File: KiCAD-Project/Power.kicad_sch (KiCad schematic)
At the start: 19 parts, among them U401 DRV8323SRTAR-DRV8323SRTAR

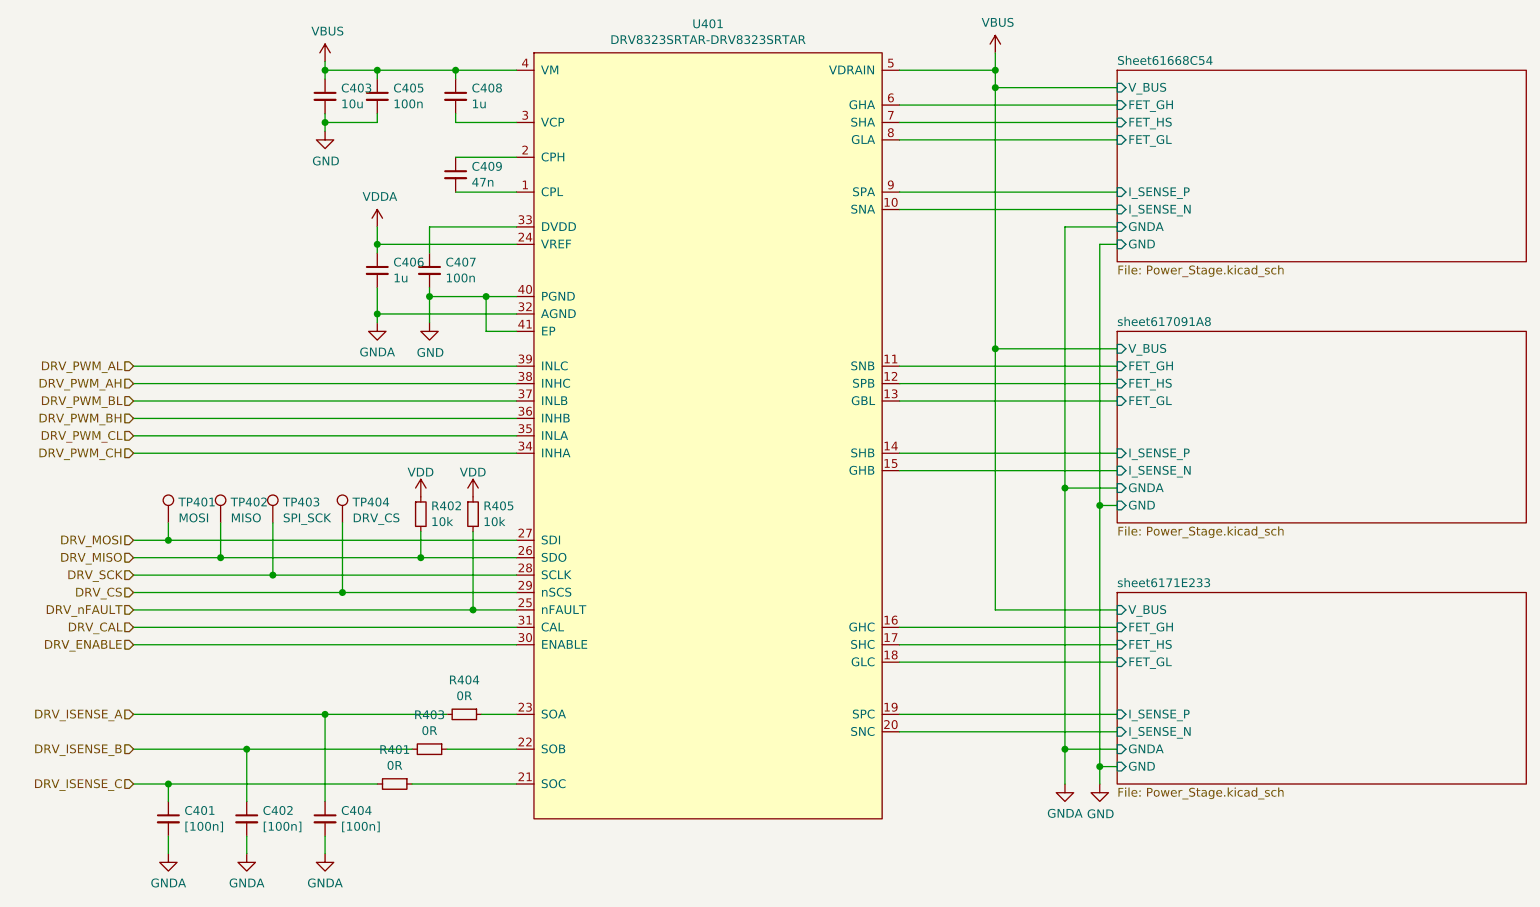
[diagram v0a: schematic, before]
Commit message: DRC resolved
removed GNDA, GNDS from schematic due to no solution was found to get a net-tie in inner layers
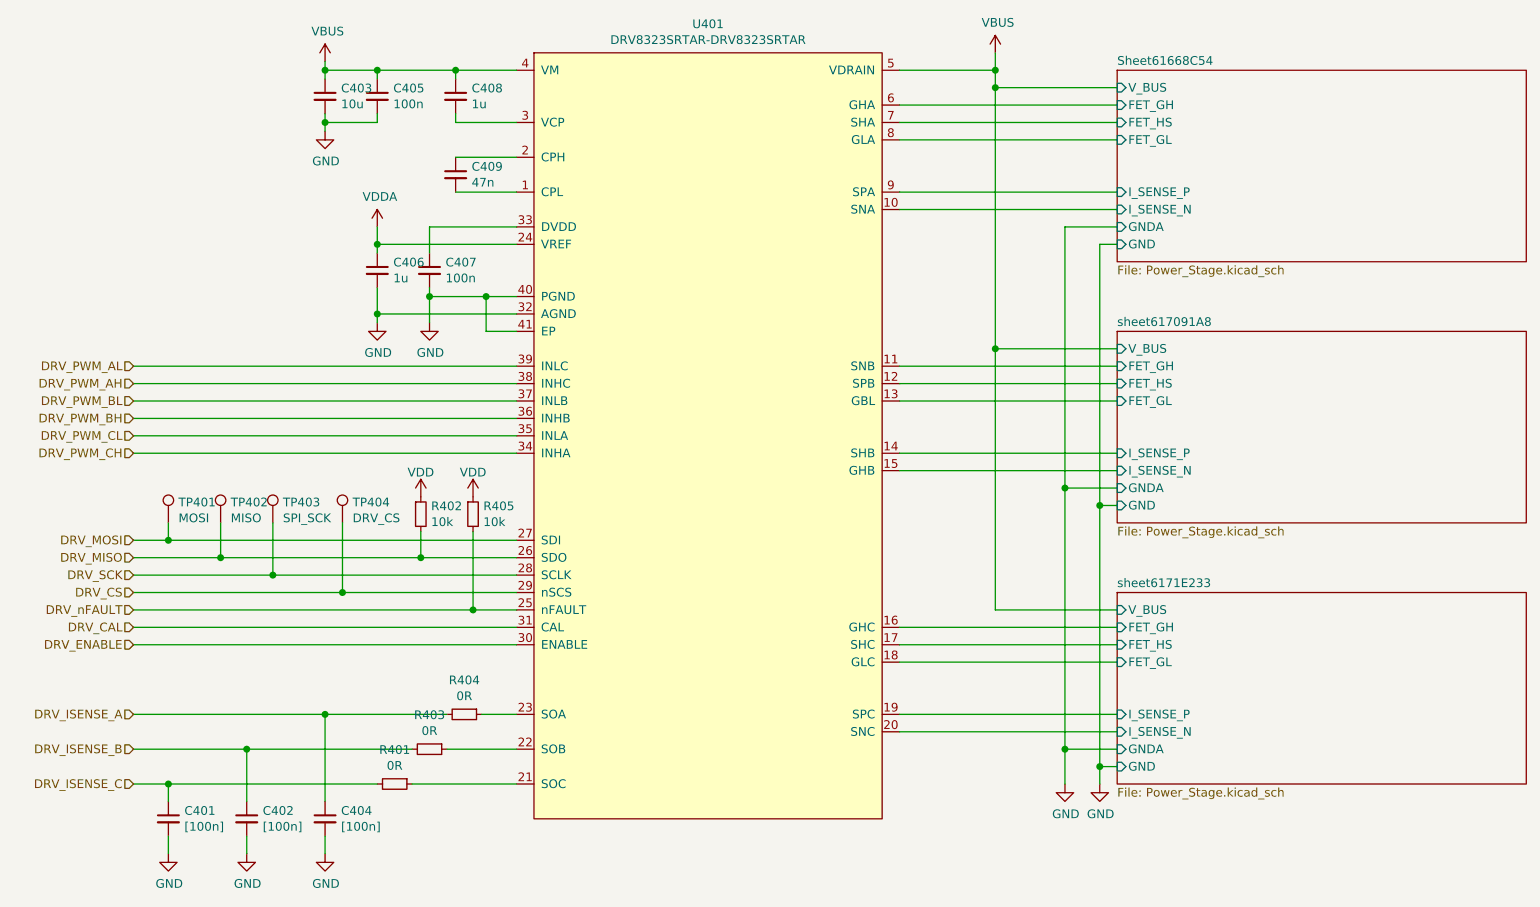
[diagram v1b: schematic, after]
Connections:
- net GNDA is gone; now on net GND: C401.2, C402.2, C404.2, C406.2, U401.32 (AGND)
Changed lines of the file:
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@@
     (pin "1")
   )
-  (symbol (lib_id "power:GNDA") (at 81.28 152.4 0) (unit 1)
-    (in_bom yes) (on_board yes) (fields_autoplaced)
-    (property "Reference" "#PWR0132" (id 0) (at 81.28 158.75 0)
+  (symbol (lib_id "power:GND") (at 81.28 152.4 0) (unit 1)
+    (in_bom yes) (on_board yes)
+    (property "Reference" "#PWR?" (id 0) (at 81.28 158.75 0)
       (effects (font (size 1.27 1.27)) hide)
     )
-    (property "Value" "GNDA" (id 1) (at 81.28 156.7244 0))
+    (property "Value" "GND" (id 1) (at 81.407 156.7942 0))
     (property "Footprint" "" (id 2) (at 81.28 152.4 0)
       (effects (font (size 1.27 1.27)) hide)
@@
     (pin "1")
   )
-  (symbol (lib_id "power:GNDA") (at 92.71 152.4 0) (unit 1)
-    (in_bom yes) (on_board yes) (fields_autoplaced)
-    (property "Reference" "#PWR0133" (id 0) (at 92.71 158.75 0)
+  (symbol (lib_id "power:GND") (at 92.71 152.4 0) (unit 1)
+    (in_bom yes) (on_board yes)
+    (property "Reference" "#PWR?" (id 0) (at 92.71 158.75 0)
       (effects (font (size 1.27 1.27)) hide)
     )
-    (property "Value" "GNDA" (id 1) (at 92.71 156.7244 0))
+    (property "Value" "GND" (id 1) (at 92.837 156.7942 0))
     (property "Footprint" "" (id 2) (at 92.71 152.4 0)
       (effects (font (size 1.27 1.27)) hide)
@@
     (pin "1")
   )
-  (symbol (lib_id "power:GNDA") (at 104.14 152.4 0) (unit 1)
-    (in_bom yes) (on_board yes) (fields_autoplaced)
-    (property "Reference" "#PWR0134" (id 0) (at 104.14 158.75 0)
+  (symbol (lib_id "power:GND") (at 104.14 152.4 0) (unit 1)
+    (in_bom yes) (on_board yes)
+    (property "Reference" "#PWR?" (id 0) (at 104.14 158.75 0)
       (effects (font (size 1.27 1.27)) hide)
     )
-    (property "Value" "GNDA" (id 1) (at 104.14 156.7244 0))
+    (property "Value" "GND" (id 1) (at 104.267 156.7942 0))
     (property "Footprint" "" (id 2) (at 104.14 152.4 0)
       (effects (font (size 1.27 1.27)) hide)
@@
     (pin "1")
   )
-  (symbol (lib_id "power:GNDA") (at 111.76 74.93 0) (unit 1)
-    (in_bom yes) (on_board yes) (fields_autoplaced)
-    (property "Reference" "#PWR0131" (id 0) (at 111.76 81.28 0)
+  (symbol (lib_id "power:GND") (at 111.76 74.93 0) (unit 1)
+    (in_bom yes) (on_board yes)
+    (property "Reference" "#PWR?" (id 0) (at 111.76 81.28 0)
       (effects (font (size 1.27 1.27)) hide)
     )
-    (property "Value" "GNDA" (id 1) (at 111.76 79.2544 0))
+    (property "Value" "GND" (id 1) (at 111.887 79.3242 0))
     (property "Footprint" "" (id 2) (at 111.76 74.93 0)
       (effects (font (size 1.27 1.27)) hide)
@@
     (pin "1")
   )
-  (symbol (lib_id "power:GNDA") (at 212.09 142.24 0) (unit 1)
-    (in_bom yes) (on_board yes) (fields_autoplaced)
-    (property "Reference" "#PWR0101" (id 0) (at 212.09 148.59 0)
+  (symbol (lib_id "power:GND") (at 212.09 142.24 0) (unit 1)
+    (in_bom yes) (on_board yes)
+    (property "Reference" "#PWR?" (id 0) (at 212.09 148.59 0)
       (effects (font (size 1.27 1.27)) hide)
     )
-    (property "Value" "GNDA" (id 1) (at 212.09 146.5644 0))
+    (property "Value" "GND" (id 1) (at 212.217 146.6342 0))
     (property "Footprint" "" (id 2) (at 212.09 142.24 0)
       (effects (font (size 1.27 1.27)) hide)

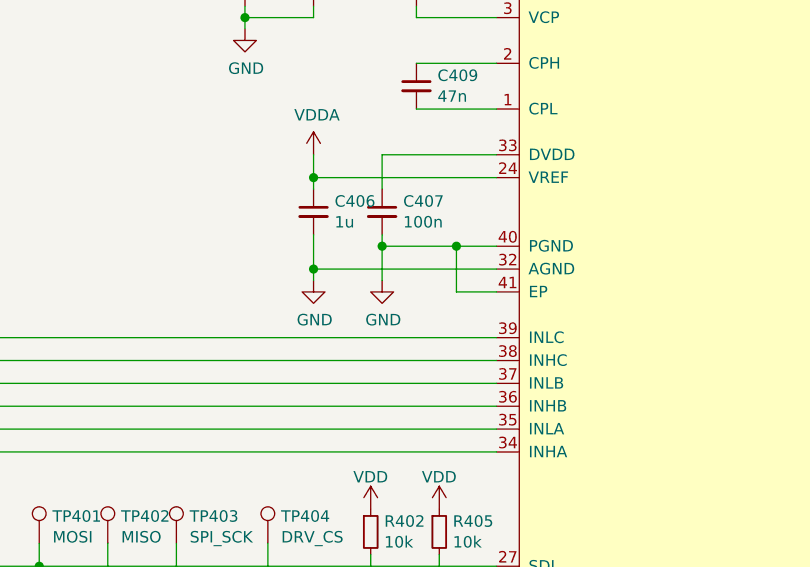
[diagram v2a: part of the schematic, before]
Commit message: changed connectors to THT
changed connectors to THT, removed UART connector
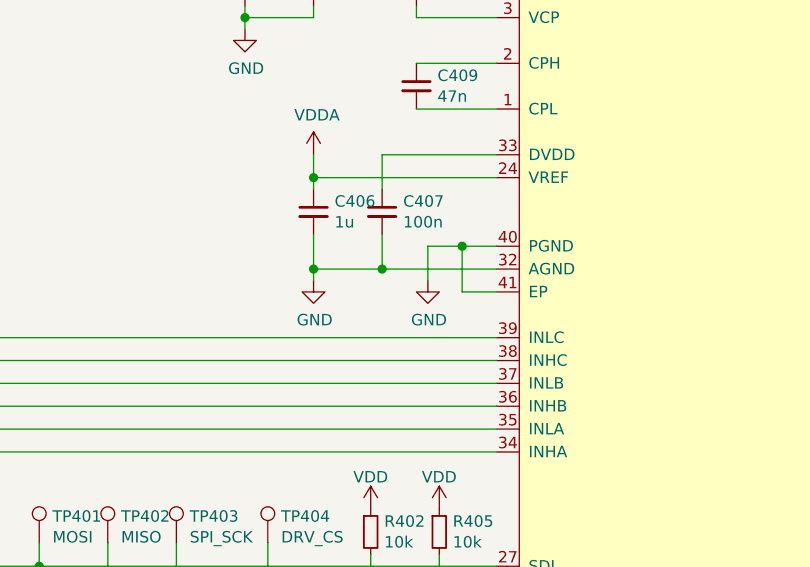
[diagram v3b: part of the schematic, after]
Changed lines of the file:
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@@
   (junction (at 111.76 73.66) (diameter 1.016) (color 0 0 0 0))
   (junction (at 118.11 109.22) (diameter 1.016) (color 0 0 0 0))
-  (junction (at 119.38 71.12) (diameter 1.016) (color 0 0 0 0))
+  (junction (at 119.38 73.66) (diameter 1.016) (color 0 0 0 0))
   (junction (at 123.19 38.1) (diameter 1.016) (color 0 0 0 0))
   (junction (at 125.73 116.84) (diameter 1.016) (color 0 0 0 0))
-  (junction (at 127.635 71.12) (diameter 1.016) (color 0 0 0 0))
+  (junction (at 128.27 71.12) (diameter 1.016) (color 0 0 0 0))
   (junction (at 201.93 38.1) (diameter 1.016) (color 0 0 0 0))
   (junction (at 201.93 40.64) (diameter 1.016) (color 0 0 0 0))
@@
     (stroke (width 0) (type solid) (color 0 0 0 0))
   )
-  (wire (pts (xy 111.76 73.66) (xy 132.08 73.66))
+  (wire (pts (xy 111.76 73.66) (xy 119.38 73.66))
     (stroke (width 0) (type solid) (color 0 0 0 0))
   )
@@
     (stroke (width 0) (type solid) (color 0 0 0 0))
   )
-  (wire (pts (xy 119.38 69.85) (xy 119.38 71.12))
-    (stroke (width 0) (type solid) (color 0 0 0 0))
-  )
-  (wire (pts (xy 119.38 71.12) (xy 119.38 74.93))
-    (stroke (width 0) (type solid) (color 0 0 0 0))
-  )
-  (wire (pts (xy 119.38 71.12) (xy 127.635 71.12))
+  (wire (pts (xy 119.38 69.85) (xy 119.38 73.66))
+    (stroke (width 0) (type solid) (color 0 0 0 0))
+  )
+  (wire (pts (xy 119.38 73.66) (xy 132.08 73.66))
     (stroke (width 0) (type solid) (color 0 0 0 0))
   )
@@
     (stroke (width 0) (type solid) (color 0 0 0 0))
   )
+  (wire (pts (xy 124.46 71.12) (xy 128.27 71.12))
+    (stroke (width 0) (type solid) (color 0 0 0 0))
+  )
+  (wire (pts (xy 124.46 74.93) (xy 124.46 71.12))
+    (stroke (width 0) (type solid) (color 0 0 0 0))
+  )
   (wire (pts (xy 125.73 105.41) (xy 125.73 116.84))
     (stroke (width 0) (type solid) (color 0 0 0 0))
@@
     (stroke (width 0) (type solid) (color 0 0 0 0))
   )
-  (wire (pts (xy 127.635 71.12) (xy 132.08 71.12))
-    (stroke (width 0) (type solid) (color 0 0 0 0))
-  )
-  (wire (pts (xy 127.635 76.2) (xy 127.635 71.12))
-    (stroke (width 0) (type solid) (color 0 0 0 0))
-  )
-  (wire (pts (xy 127.635 76.2) (xy 132.08 76.2))
+  (wire (pts (xy 128.27 71.12) (xy 132.08 71.12))
+    (stroke (width 0) (type solid) (color 0 0 0 0))
+  )
+  (wire (pts (xy 128.27 76.2) (xy 128.27 71.12))
+    (stroke (width 0) (type solid) (color 0 0 0 0))
+  )
+  (wire (pts (xy 128.27 76.2) (xy 132.08 76.2))
     (stroke (width 0) (type solid) (color 0 0 0 0))
   )
@@
   (symbol (lib_id "power:VDDA") (at 111.76 60.96 0) (unit 1)
     (in_bom yes) (on_board yes)
-    (property "Reference" "#PWR0407" (id 0) (at 111.76 64.77 0)
+    (property "Reference" "#PWR0406" (id 0) (at 111.76 64.77 0)
       (effects (font (size 1.27 1.27)) hide)
     )
@@
   (symbol (lib_id "power:VDD") (at 118.11 100.33 0) (unit 1)
     (in_bom yes) (on_board yes) (fields_autoplaced)
-    (property "Reference" "#PWR0143" (id 0) (at 118.11 104.14 0)
+    (property "Reference" "#PWR0408" (id 0) (at 118.11 104.14 0)
       (effects (font (size 1.27 1.27)) hide)
     )
@@
   (symbol (lib_id "power:VDD") (at 125.73 100.33 0) (unit 1)
     (in_bom yes) (on_board yes) (fields_autoplaced)
-    (property "Reference" "#PWR0141" (id 0) (at 125.73 104.14 0)
+    (property "Reference" "#PWR0410" (id 0) (at 125.73 104.14 0)
       (effects (font (size 1.27 1.27)) hide)
     )
@@
   (symbol (lib_id "power:VBUS") (at 201.93 35.56 0) (unit 1)
     (in_bom yes) (on_board yes)
-    (property "Reference" "#PWR0410" (id 0) (at 201.93 39.37 0)
+    (property "Reference" "#PWR0411" (id 0) (at 201.93 39.37 0)
       (effects (font (size 1.27 1.27)) hide)
     )
@@
   (symbol (lib_id "power:GND") (at 81.28 152.4 0) (unit 1)
     (in_bom yes) (on_board yes)
-    (property "Reference" "#PWR030" (id 0) (at 81.28 158.75 0)
+    (property "Reference" "#PWR0401" (id 0) (at 81.28 158.75 0)
       (effects (font (size 1.27 1.27)) hide)
     )
@@
   (symbol (lib_id "power:GND") (at 92.71 152.4 0) (unit 1)
     (in_bom yes) (on_board yes)
-    (property "Reference" "#PWR031" (id 0) (at 92.71 158.75 0)
+    (property "Reference" "#PWR0402" (id 0) (at 92.71 158.75 0)
       (effects (font (size 1.27 1.27)) hide)
     )
@@
   (symbol (lib_id "power:GND") (at 104.14 152.4 0) (unit 1)
     (in_bom yes) (on_board yes)
-    (property "Reference" "#PWR032" (id 0) (at 104.14 158.75 0)
+    (property "Reference" "#PWR0405" (id 0) (at 104.14 158.75 0)
       (effects (font (size 1.27 1.27)) hide)
     )
@@
   (symbol (lib_id "power:GND") (at 111.76 74.93 0) (unit 1)
     (in_bom yes) (on_board yes)
-    (property "Reference" "#PWR033" (id 0) (at 111.76 81.28 0)
+    (property "Reference" "#PWR0407" (id 0) (at 111.76 81.28 0)
       (effects (font (size 1.27 1.27)) hide)
     )
@@
     (pin "1")
   )
-  (symbol (lib_id "power:GND") (at 119.38 74.93 0) (unit 1)
-    (in_bom yes) (on_board yes)
-    (property "Reference" "#PWR0406" (id 0) (at 119.38 81.28 0)
-      (effects (font (size 1.27 1.27)) hide)
-    )
-    (property "Value" "GND" (id 1) (at 119.507 79.3242 0))
-    (property "Footprint" "" (id 2) (at 119.38 74.93 0)
-      (effects (font (size 1.27 1.27)) hide)
-    )
-    (property "Datasheet" "" (id 3) (at 119.38 74.93 0)
+  (symbol (lib_id "power:GND") (at 124.46 74.93 0) (unit 1)
+    (in_bom yes) (on_board yes)
+    (property "Reference" "#PWR0409" (id 0) (at 124.46 81.28 0)
+      (effects (font (size 1.27 1.27)) hide)
+    )
+    (property "Value" "GND" (id 1) (at 124.587 79.3242 0))
+    (property "Footprint" "" (id 2) (at 124.46 74.93 0)
+      (effects (font (size 1.27 1.27)) hide)
+    )
+    (property "Datasheet" "" (id 3) (at 124.46 74.93 0)
       (effects (font (size 1.27 1.27)) hide)
     )
@@
   (symbol (lib_id "power:GND") (at 212.09 142.24 0) (unit 1)
     (in_bom yes) (on_board yes)
-    (property "Reference" "#PWR034" (id 0) (at 212.09 148.59 0)
+    (property "Reference" "#PWR0412" (id 0) (at 212.09 148.59 0)
       (effects (font (size 1.27 1.27)) hide)
     )
@@
   (symbol (lib_id "power:GND") (at 217.17 142.24 0) (unit 1)
     (in_bom yes) (on_board yes)
-    (property "Reference" "#PWR0411" (id 0) (at 217.17 148.59 0)
-      (effects (font (size 1.27 1.27)) hide)
-    )
+    (property "Reference" "#PWR0413" (id 0) (at 217.17 148.59 0)
+      (effects (font (size 1.27 1.27)) hide)
+    )
